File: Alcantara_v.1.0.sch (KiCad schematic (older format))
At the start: 22 parts, among them IC3 TLV803EA30DCKR, J5 PJS008U-3000-0, J8 53261-0527, Q1 MMSS8050-H-TP, Q2 MMSS8050-H-TP

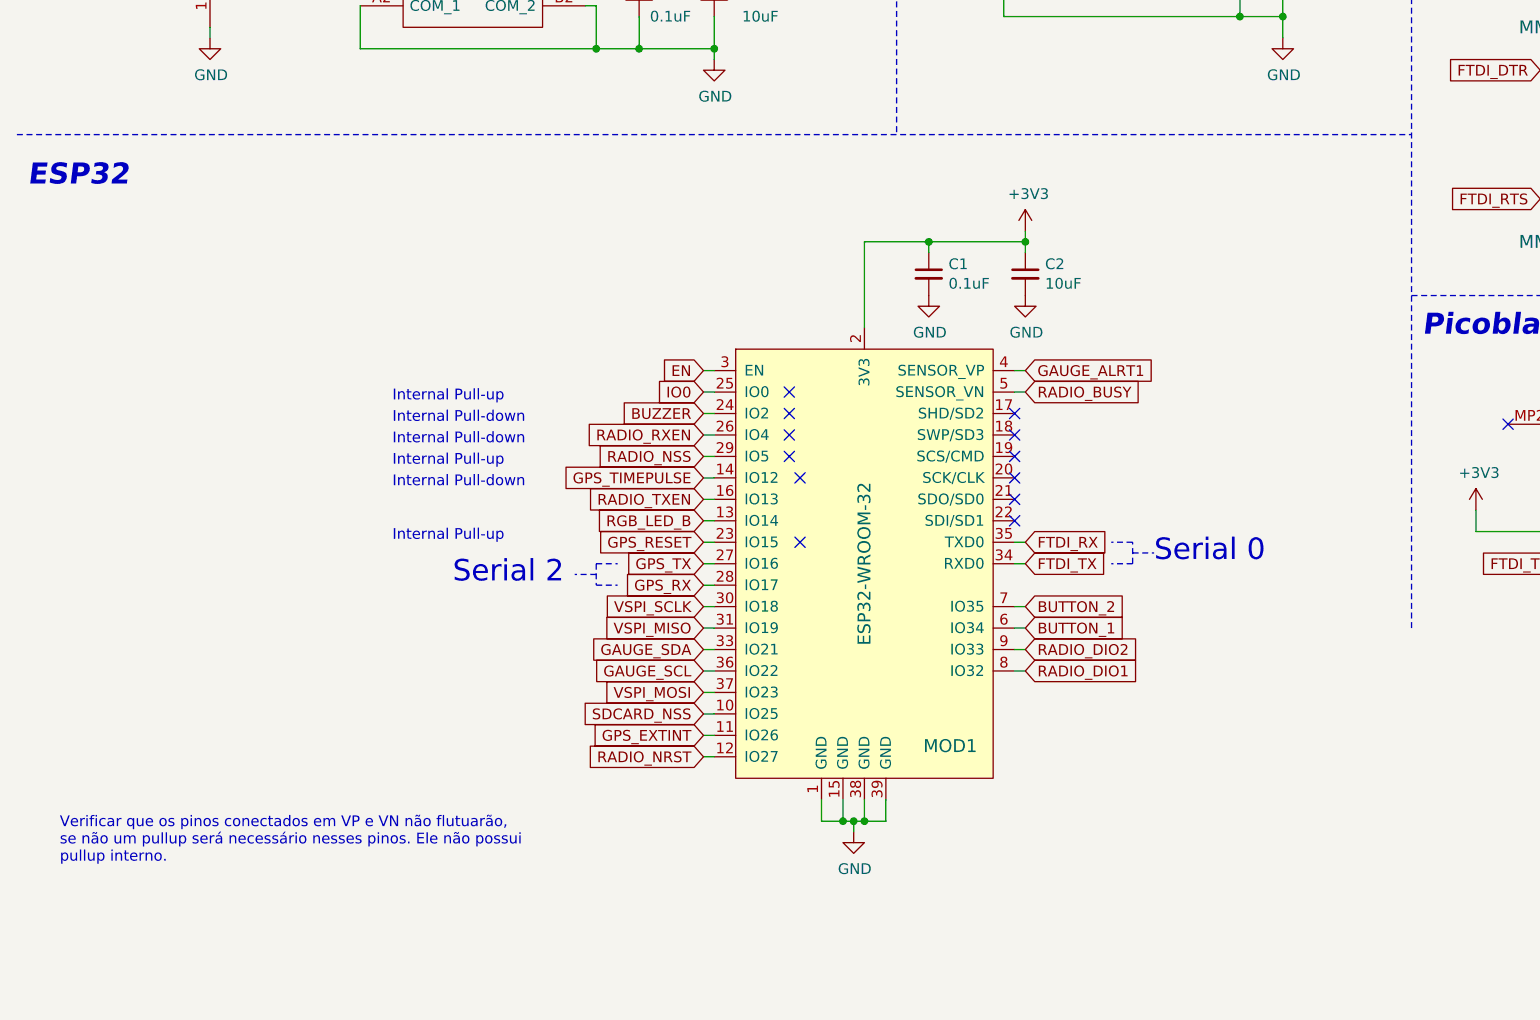
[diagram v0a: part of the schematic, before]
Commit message: Updated silk screens and components 3D models
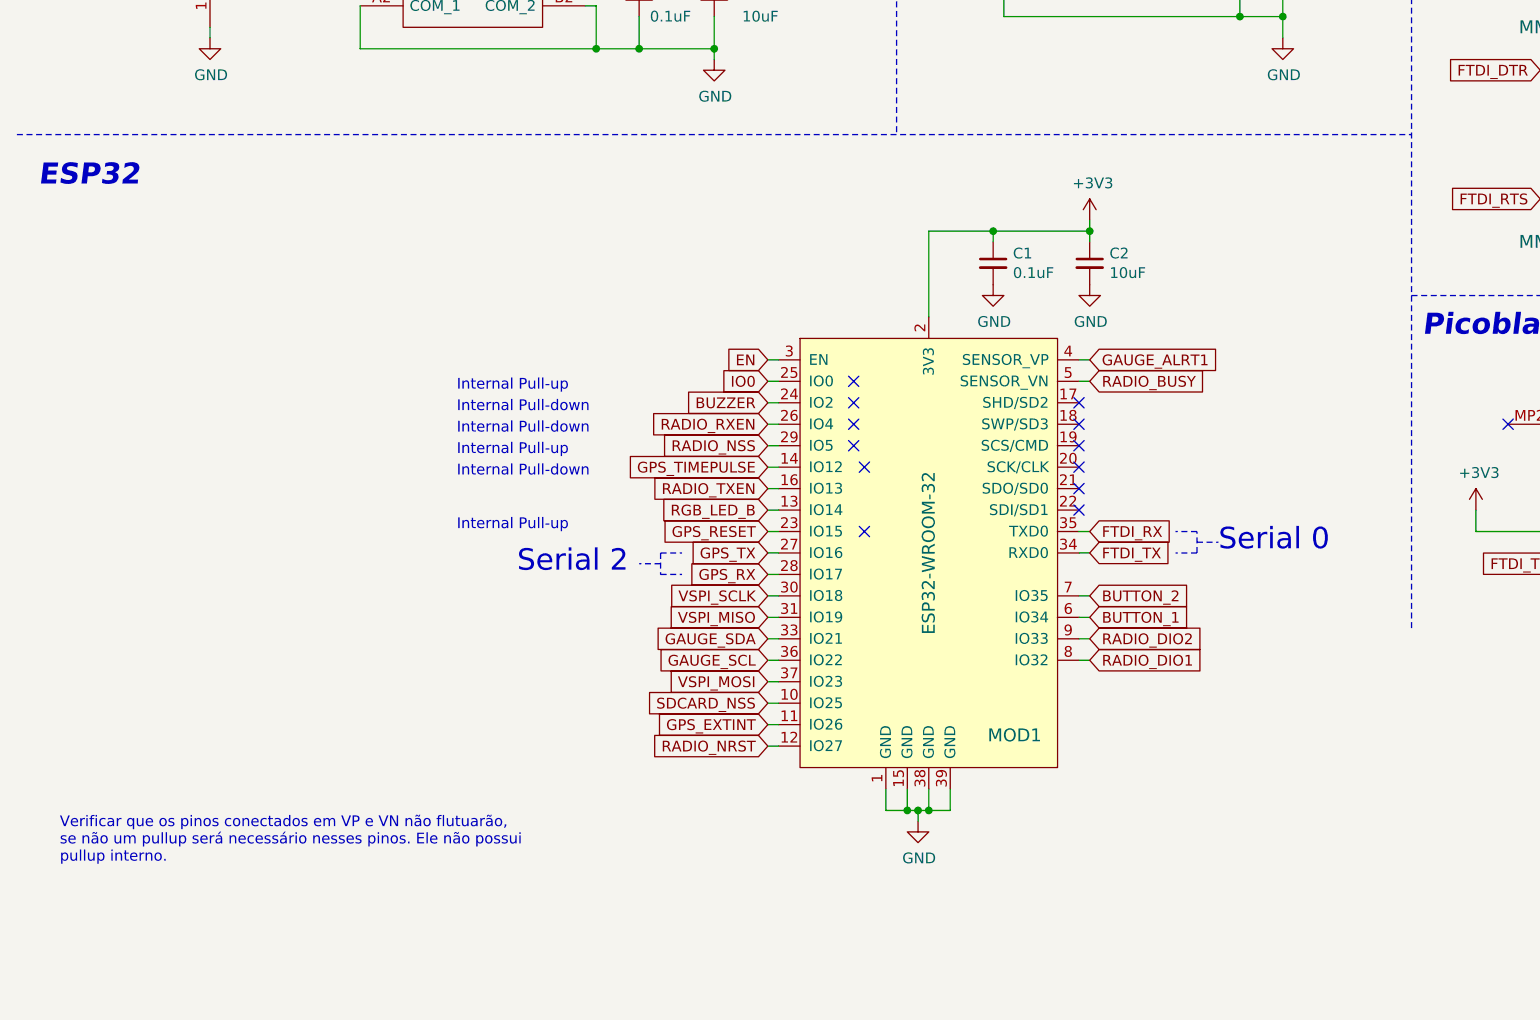
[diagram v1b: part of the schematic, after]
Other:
- moved on the sheet: C1, C2, MOD1

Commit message: Updated RF section ground planes.
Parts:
- removed R8: 10K, Resistor_SMD:R_0603_1608Metric, symbol Device:R_Small
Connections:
- net GPS_TIMEPULSE renamed GPS_ON_OFF
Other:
- note added: "Os resistores de pull-up ou pull-down devem ser utilizados um\npor vez, dependendo da tensão da flash interna da ESP.\nNote que os resistores que atuam como pull-down estão na\npágina "Tecommunications" pois lá eles são os resistores do\nMosfet que aciona o GPS.\n\nIsso ocorre pois o pino 12 é um pino lido no boot para selecionar\na tensão que alimenta a flash interna: \n1 -> 1.8V\n0 -> 3.3V\n\nS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"
- note removed: "Os resistores de pull-up ou pull-down devem ser utilizados um\npor vez, dependendo da tensão da flash interna da ESP.\n\nIsso ocorre pois o pino 12 é um pino lido no boot para selecionar\na tensão que alimenta a flash interna: \n1 -> 1.8V\n0 -> 3.3V\n\nLer mais sobre aqui:\nhttps://docs.espressif.com/projects/esp-idf/en/\nlatest/esp32/api-reference/peripherals/sd_pullup_requirements.\nhtml#no-pul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"
- moved on the sheet: R6
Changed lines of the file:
@@
 F4 "GPS_EXTINT" I L 9850 2250 50
 F5 "GPS_RESET" I L 9850 2400 50
-F6 "GPS_TIMEPULSE" I L 9850 2550 50
-F7 "RADIO_MOSI" I L 9850 2800 50
-F8 "RADIO_MISO" I L 9850 3100 50
-F9 "RADIO_NRST" I L 9850 3400 50
-F10 "RADIO_BUSY" I L 9850 3550 50
-F11 "RADIO_DIO1" I L 9850 3700 50
-F12 "RADIO_DIO2" I L 9850 3850 50
-F13 "RADIO_TXEN" I L 9850 4000 50
-F14 "RADIO_RXEN" I L 9850 4150 50
-F15 "RADIO_NSS" I L 9850 2950 50
-F16 "RADIO_SCK" I L 9850 3250 50
+F6 "RADIO_MOSI" I L 9850 2800 50
+F7 "RADIO_MISO" I L 9850 3100 50
+F8 "RADIO_NRST" I L 9850 3400 50
+F9 "RADIO_BUSY" I L 9850 3550 50
+F10 "RADIO_DIO1" I L 9850 3700 50
+F11 "RADIO_DIO2" I L 9850 3850 50
+F12 "RADIO_TXEN" I L 9850 4000 50
+F13 "RADIO_RXEN" I L 9850 4150 50
+F14 "RADIO_NSS" I L 9850 2950 50
+F15 "RADIO_SCK" I L 9850 3250 50
+F16 "GPS_ON_OFF" I L 9850 2550 50
 $EndSheet
 $Sheet
@@
 	9750 2400 9850 2400
 Text GLabel 9750 2550 0    50   Input ~ 0
-GPS_TIMEPULSE
+GPS_ON_OFF
 Wire Wire Line
 	9750 2550 9850 2550
@@
 > Ou ligar junto ao RGB principal
 Text GLabel 4000 5750 0    50   Input ~ 0
-GPS_TIMEPULSE
+GPS_ON_OFF
 Text GLabel 4000 6850 0    50   Input ~ 0
 SDCARD_NSS
@@
 	2250 1750 1800 1750
 Wire Wire Line
-	8100 1600 8300 1600
+	8375 1650 8575 1650
 $Comp
 L Device:R_Small R6
 U 1 1 61313692
-P 8300 1400
-F 0 "R6" V 8104 1400 50  0000 C CNN
-F 1 "10K" V 8195 1400 50  0000 C CNN
-F 2 "Resistor_SMD:R_0603_1608Metric" H 8300 1400 50  0001 C CNN
-F 3 "~" H 8300 1400 50  0001 C CNN
-	1    8300 1400
-	1    0    0    -1
-$EndComp
-$Comp
-L Device:R_Small R8
-U 1 1 61313698
-P 8300 1800
-F 0 "R8" V 8104 1800 50  0000 C CNN
-F 1 "10K" V 8195 1800 50  0000 C CNN
-F 2 "Resistor_SMD:R_0603_1608Metric" H 8300 1800 50  0001 C CNN
-F 3 "~" H 8300 1800 50  0001 C CNN
-	1    8300 1800
-	1    0    0    -1
-$EndComp
-Wire Wire Line
-	8300 1600 8300 1500
-Wire Wire Line
-	8300 1600 8300 1700
-Connection ~ 8300 1600
+P 8575 1450
+F 0 "R6" V 8379 1450 50  0000 C CNN
+F 1 "10K" V 8470 1450 50  0000 C CNN
+F 2 "Resistor_SMD:R_0603_1608Metric" H 8575 1450 50  0001 C CNN
+F 3 "~" H 8575 1450 50  0001 C CNN
+	1    8575 1450
+	1    0    0    -1
+$EndComp
+Wire Wire Line
+	8575 1650 8575 1550
 $Comp
 L power:+3V3 #PWR0105
 U 1 1 6134BA7C
-P 8300 1200
-F 0 "#PWR0105" H 8300 1050 50  0001 C CNN
-F 1 "+3V3" H 8315 1373 50  0000 C CNN
-F 2 "" H 8300 1200 50  0001 C CNN
-F 3 "" H 8300 1200 50  0001 C CNN
-	1    8300 1200
-	1    0    0    -1
-$EndComp
-$Comp
-L power:GND #PWR0106
-U 1 1 6134BDD8
-P 8300 2000
-F 0 "#PWR0106" H 8300 1750 50  0001 C CNN
-F 1 "GND" H 8305 1827 50  0000 C CNN
-F 2 "" H 8300 2000 50  0001 C CNN
-F 3 "" H 8300 2000 50  0001 C CNN
-	1    8300 2000
-	1    0    0    -1
-$EndComp
-Wire Wire Line
-	8300 2000 8300 1900
-Wire Wire Line
-	8300 1300 8300 1200
-Text Notes 5150 2000 0    50   ~ 0
-Os resistores de pull-up ou pull-down devem ser utilizados um\npor vez, dependendo da tensão da flash interna da ESP.\n\nIsso ocorre pois o pino 12 é um pino lido no boot para selecionar\na tensão que alimenta a flash interna: \n1 -> 1.8V\n0 -> 3.3V\n\nLer mais sobre aqui:\nhttps://docs.espressif.com/projects/esp-idf/en/\nlatest/esp32/api-reference/peripherals/sd_pullup_requirements.\nhtml#no-pull-up-on-gpio12
+P 8575 1250
+F 0 "#PWR0105" H 8575 1100 50  0001 C CNN
+F 1 "+3V3" H 8590 1423 50  0000 C CNN
+F 2 "" H 8575 1250 50  0001 C CNN
+F 3 "" H 8575 1250 50  0001 C CNN
+	1    8575 1250
+	1    0    0    -1
+$EndComp
+Wire Wire Line
+	8575 1350 8575 1250
+Text Notes 4875 2450 0    47   ~ 0
+Os resistores de pull-up ou pull-down devem ser utilizados um\npor vez, dependendo da tensão da flash interna da ESP.\nNote que os resistores que atuam como pull-down estão na\npágina "Tecommunications" pois lá eles são os resistores do\nMosfet que aciona o GPS.\n\nIsso ocorre pois o pino 12 é um pino lido no boot para selecionar\na tensão que alimenta a flash interna: \n1 -> 1.8V\n0 -> 3.3V\n\nSe for necessário utilizar a flash de 3.3V (padrão) basta não utilizar\no pull-up.\n\nSe for necessário utilizar a flash de 1.8V (padrão), deve-se remover\no pull-down do gate do Mosfet, mas o sinal no GPIO12 deve ser\nbem definido (1 ou 0) quando quiser ligar ou desligar o GPS.\n\nLer mais sobre aqui:\nhttps://docs.espressif.com/projects/esp-idf/en/\nlatest/esp32/api-reference/peripherals/sd_pullup_requirements.\nhtml#no-pull-up-on-gpio12
 NoConn ~ 4400 5550
 NoConn ~ 4400 5350
@@
 Wire Wire Line
 	8150 6050 8600 6050
-Text GLabel 8100 1600 0    50   Input ~ 0
-GPS_TIMEPULSE
+Text GLabel 8375 1650 0    50   Input ~ 0
+GPS_ON_OFF
 $Comp
 L Device:R_Small R5
